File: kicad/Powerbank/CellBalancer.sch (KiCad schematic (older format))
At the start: 1 part

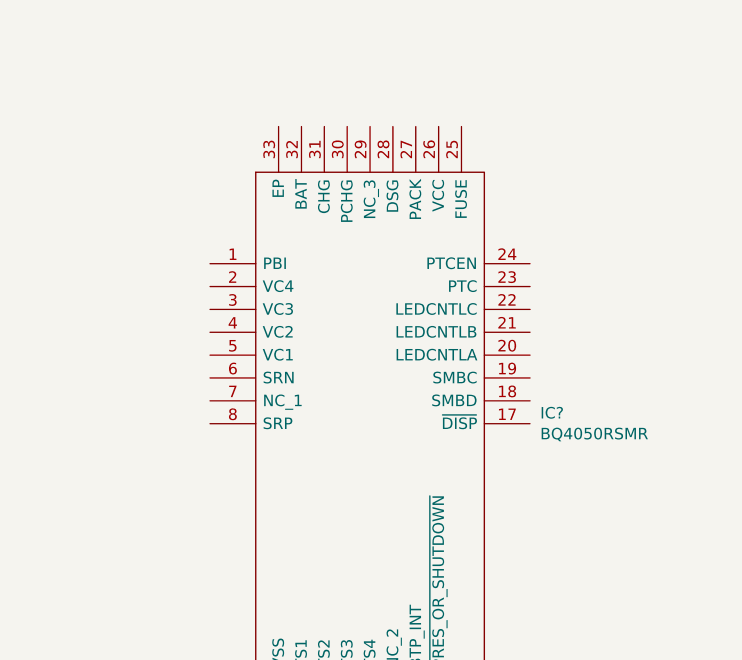
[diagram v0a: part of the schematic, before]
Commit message: Added more schematics
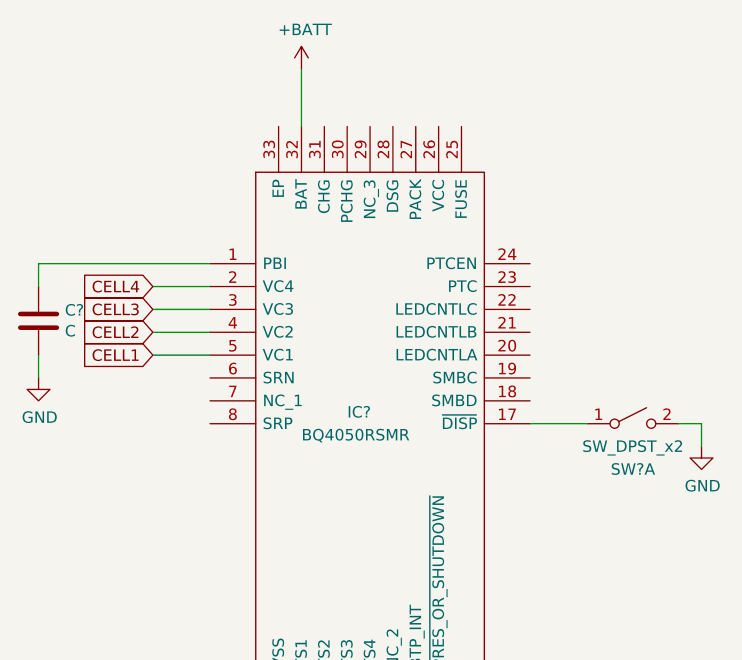
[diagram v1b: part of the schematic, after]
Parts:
- added C?: C, symbol Device:C
- added SW?: SW_DPST_x2, symbol Switch:SW_DPST_x2
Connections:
- net at IC?.1 (PBI): now also C?.2
- net at IC?.17 (~DISP): now also SW?.1 (A)
- net CELL4: now reaches IC?.2 (VC4)
- net CELL3: now reaches IC?.3 (VC3)
- net +BATT: now reaches IC?.32 (BAT)
- net CELL2: now reaches IC?.4 (VC2)
- net CELL1: now reaches IC?.5 (VC1)
- new net GND: C?.1, SW?.2 (B)
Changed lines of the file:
@@
 $Descr A4 11693 8268
 encoding utf-8
-Sheet 2 2
+Sheet 2 7
 Title ""
 Date ""
@@
 U 1 1 5E0CC2E3
 P 5000 3350
-F 0 "IC?" H 6444 2696 50  0000 L CNN
-F 1 "BQ4050RSMR" H 6444 2605 50  0000 L CNN
+F 0 "IC?" H 5600 2700 50  0000 L CNN
+F 1 "BQ4050RSMR" H 5400 2600 50  0000 L CNN
 F 2 "QFN40P400X400X100-33N-D" H 6250 3750 50  0001 L CNN
 F 3 "http://www.ti.com/lit/gpn/bq4050" H 6250 3650 50  0001 L CNN
@@
 	1    0    0    -1
 $EndComp
+$Comp
+L power:+BATT #PWR?
+U 1 1 5E0D5CE8
+P 5400 2500
+F 0 "#PWR?" H 5400 2350 50  0001 C CNN
+F 1 "+BATT" H 5415 2673 50  0000 C CNN
+F 2 "" H 5400 2500 50  0001 C CNN
+F 3 "" H 5400 2500 50  0001 C CNN
+	1    5400 2500
+	1    0    0    -1
+$EndComp
+Wire Wire Line
+	5400 2500 5400 2750
+Text GLabel 4750 3750 0    50   Input ~ 0
+CELL1
+Wire Wire Line
+	4750 3750 5000 3750
+Text GLabel 4750 3650 0    50   Input ~ 0
+CELL2
+Text GLabel 4750 3550 0    50   Input ~ 0
+CELL3
+Text GLabel 4750 3450 0    50   Input ~ 0
+CELL4
+Wire Wire Line
+	4750 3450 5000 3450
+Wire Wire Line
+	5000 3550 4750 3550
+Wire Wire Line
+	4750 3650 5000 3650
+$Comp
+L power:GND #PWR?
+U 1 1 5E0D64F8
+P 4250 3850
+F 0 "#PWR?" H 4250 3600 50  0001 C CNN
+F 1 "GND" H 4255 3677 50  0000 C CNN
+F 2 "" H 4250 3850 50  0001 C CNN
+F 3 "" H 4250 3850 50  0001 C CNN
+	1    4250 3850
+	1    0    0    -1
+$EndComp
+$Comp
+L Device:C C?
+U 1 1 5E0D68C3
+P 4250 3600
+F 0 "C?" H 4135 3554 50  0000 R CNN
+F 1 "C" H 4135 3645 50  0000 R CNN
+F 2 "" H 4288 3450 50  0001 C CNN
+F 3 "~" H 4250 3600 50  0001 C CNN
+	1    4250 3600
+	-1   0    0    1
+$EndComp
+Wire Wire Line
+	4250 3850 4250 3750
+Wire Wire Line
+	4250 3450 4250 3350
+Wire Wire Line
+	4250 3350 5000 3350
+$Comp
+L Switch:SW_DPST_x2 SW?
+U 1 1 5E0D80CF
+P 6850 4050
+F 0 "SW?" H 6850 3850 50  0000 C CNN
+F 1 "SW_DPST_x2" H 6850 3950 50  0000 C CNN
+F 2 "" H 6850 4050 50  0001 C CNN
+F 3 "~" H 6850 4050 50  0001 C CNN
+	1    6850 4050
+	1    0    0    -1
+$EndComp
+$Comp
+L power:GND #PWR?
+U 1 1 5E0D9358
+P 7150 4150
+F 0 "#PWR?" H 7150 3900 50  0001 C CNN
+F 1 "GND" H 7155 3977 50  0000 C CNN
+F 2 "" H 7150 4150 50  0001 C CNN
+F 3 "" H 7150 4150 50  0001 C CNN
+	1    7150 4150
+	1    0    0    -1
+$EndComp
+Wire Wire Line
+	7150 4150 7150 4050
+Wire Wire Line
+	7150 4050 7050 4050
+Wire Wire Line
+	6650 4050 6400 4050
 $EndSCHEMATC

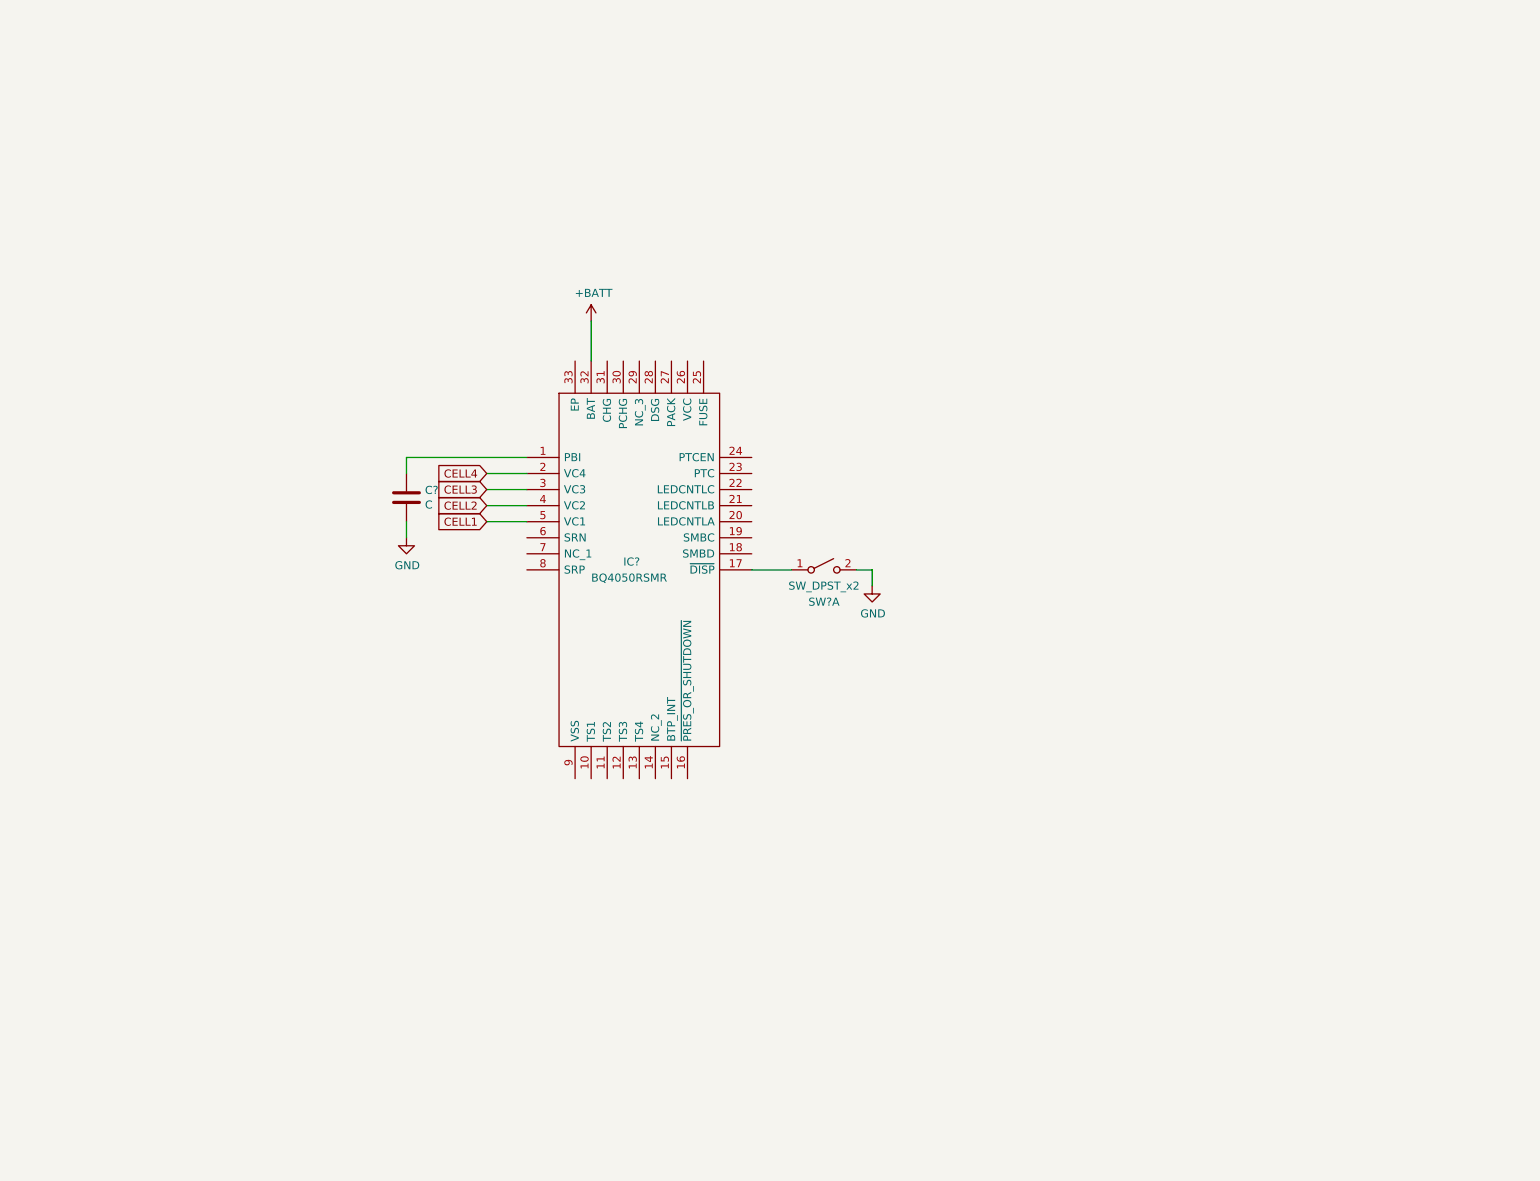
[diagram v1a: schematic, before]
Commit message: Completed cell balancer according to ref schematic
[found here](]http://www.ti.com/lit/df/tidrzn1/tidrzn1.pdf)
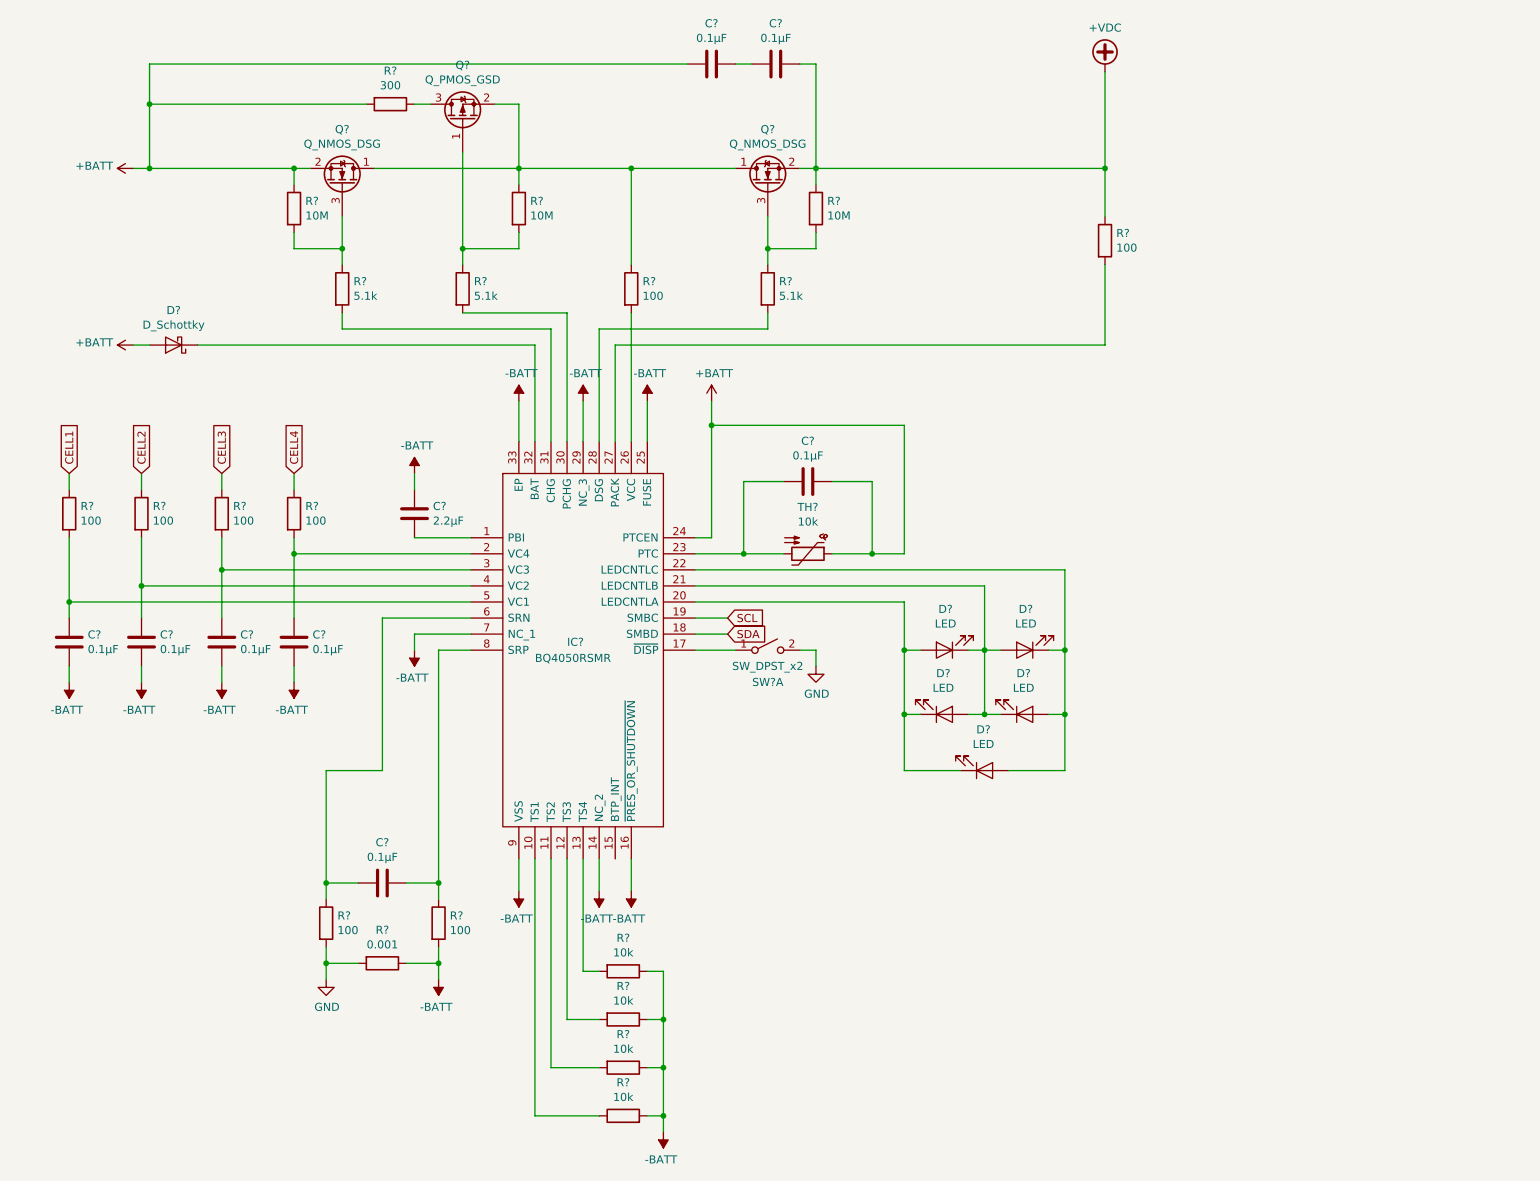
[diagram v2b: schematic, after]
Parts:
- added C? (x8): 0.1µF, symbol Device:C
- added D? (x5): LED, symbol Device:LED
- added D?: D_Schottky, symbol Device:D_Schottky
- added Q? (x2): Q_NMOS_DSG, symbol Device:Q_NMOS_DSG
- added Q?: Q_PMOS_GSD, symbol Device:Q_PMOS_GSD
- added R? (x8): 100, symbol Device:R
- added R? (x4): 10k, symbol Device:R
- added R?: 0.001, symbol Device:R
- added R? (x3): 10M, symbol Device:R
- added R? (x3): 5.1k, symbol Device:R
- added R?: 300, symbol Device:R
- added TH?: 10k, symbol Device:Thermistor_PTC
- C?: value C -> 2.2µF
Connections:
- net +BATT: now also IC?.24 (PTCEN), C?.1, C?.2, D?.2 (A), Q?.2 (S), R?.1, R?.2, TH?.1; no longer IC?.32 (BAT)
- net CELL1: now also R?.1; no longer IC?.5 (VC1)
- net CELL2: now also R?.1; no longer IC?.4 (VC2)
- net CELL3: now also R?.1; no longer IC?.3 (VC3)
- net CELL4: now also R?.1; no longer IC?.2 (VC4)
- net GND: now also R?.2, R?.2; no longer C?.1
- net at IC?.1 (PBI): now also C?.1; no longer C?.2
- net at IC?.10 (TS1): now also R?.1
- net at IC?.11 (TS2): now also R?.2
- net at IC?.12 (TS3): now also R?.2
- net at IC?.13 (TS4): now also R?.2
- net -BATT: now reaches IC?.14 (NC_2)
- net -BATT: now also C?.2, IC?.16 (~PRES_OR_SHUTDOWN), IC?.25 (FUSE), IC?.29 (NC_3), IC?.33 (EP), IC?.7 (NC_1), IC?.9 (VSS), C?.1, C?.1, C?.1, C?.1, R?.1, R?.1, R?.1, R?.1, R?.2, R?.2
- net SDA: now reaches IC?.18 (SMBD)
- net SCL: now reaches IC?.19 (SMBC)
- net at IC?.20 (LEDCNTLA): now also D?.1 (K), D?.1 (K), D?.2 (A)
- net at IC?.21 (LEDCNTLB): now also D?.1 (K), D?.1 (K), D?.2 (A), D?.2 (A)
- net at IC?.22 (LEDCNTLC): now also D?.1 (K), D?.2 (A), D?.2 (A)
- net at IC?.23 (PTC): now also C?.1, TH?.2
- net at IC?.26 (VCC): now also R?.2
- net at IC?.27 (PACK): now also R?.2
- net at IC?.28 (DSG): now also R?.2
- net at IC?.30 (PCHG): now also R?.2
- net at IC?.31 (CHG): now also R?.2
- net at IC?.6 (SRN): now also C?.1, R?.1
- net at IC?.8 (SRP): now also C?.2, R?.1
- new net: C?.2, IC?.2 (VC4), R?.2
- new net: C?.2, IC?.3 (VC3), R?.2
- new net: D?.1 (K), IC?.32 (BAT)
- new net: C?.2, IC?.4 (VC2), R?.2
- new net: C?.2, IC?.5 (VC1), R?.2
- new net: Q?.1 (D), Q?.1 (D), Q?.2 (S), R?.1, R?.1
- new net: Q?.3 (G), R?.1, R?.2 (x2)
- new net: Q?.1 (G), R?.1, R?.2
- new net: Q?.3 (D), R?.1
- new net: C?.1, C?.2
- new net +VDC: C?.2, Q?.2 (S), R?.1, R?.1
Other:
- moved on the sheet: C?, IC?, SW?A

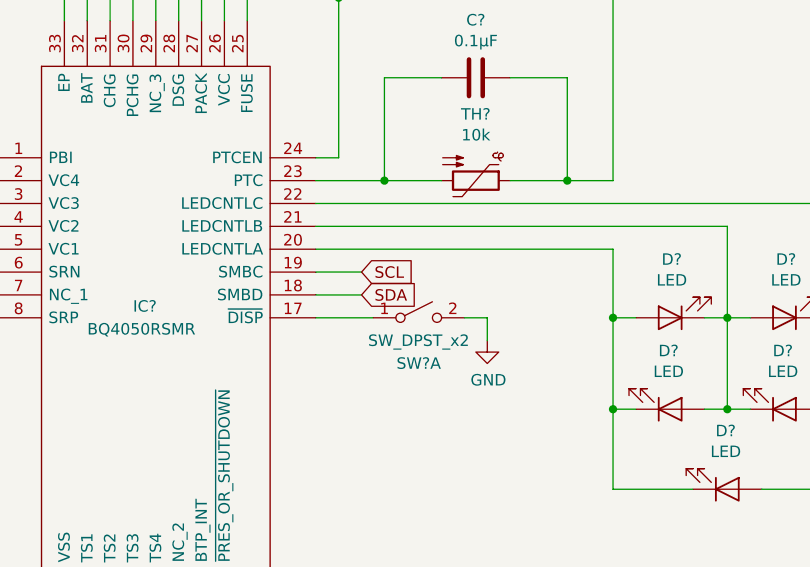
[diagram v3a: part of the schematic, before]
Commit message: Moved LDO to Buck sheet and started check of components
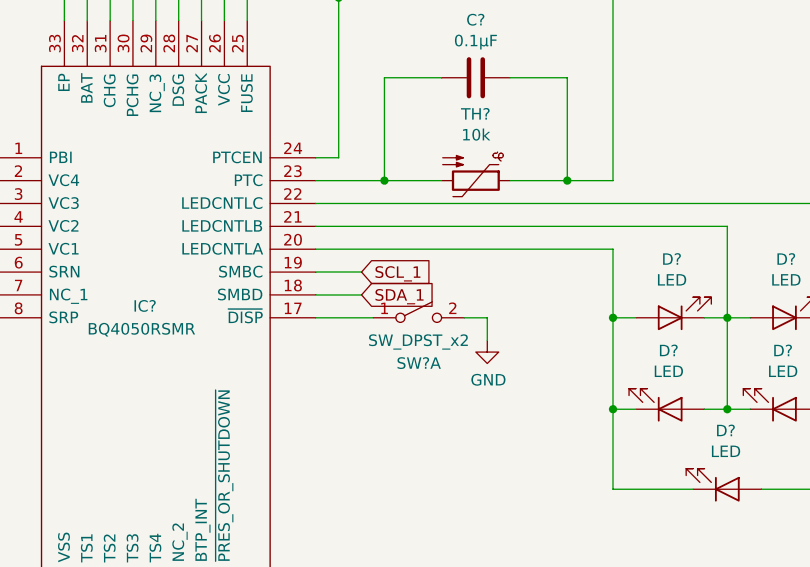
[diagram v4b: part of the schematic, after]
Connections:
- net SCL renamed SCL_1
- net SDA renamed SDA_1
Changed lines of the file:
@@
 $Descr A4 11693 8268
 encoding utf-8
-Sheet 2 8
+Sheet 2 7
 Title ""
 Date ""
@@
 Connection ~ 8350 4550
 Text GLabel 6250 4350 2    50   Input ~ 0
-SCL
+SCL_1
 Text GLabel 6250 4450 2    50   Input ~ 0
-SDA
+SDA_1
 Wire Wire Line
 	6250 4450 6050 4450
